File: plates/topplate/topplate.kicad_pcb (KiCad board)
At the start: 2 copper layers, 107.2 x 83.2 mm, 3 parts

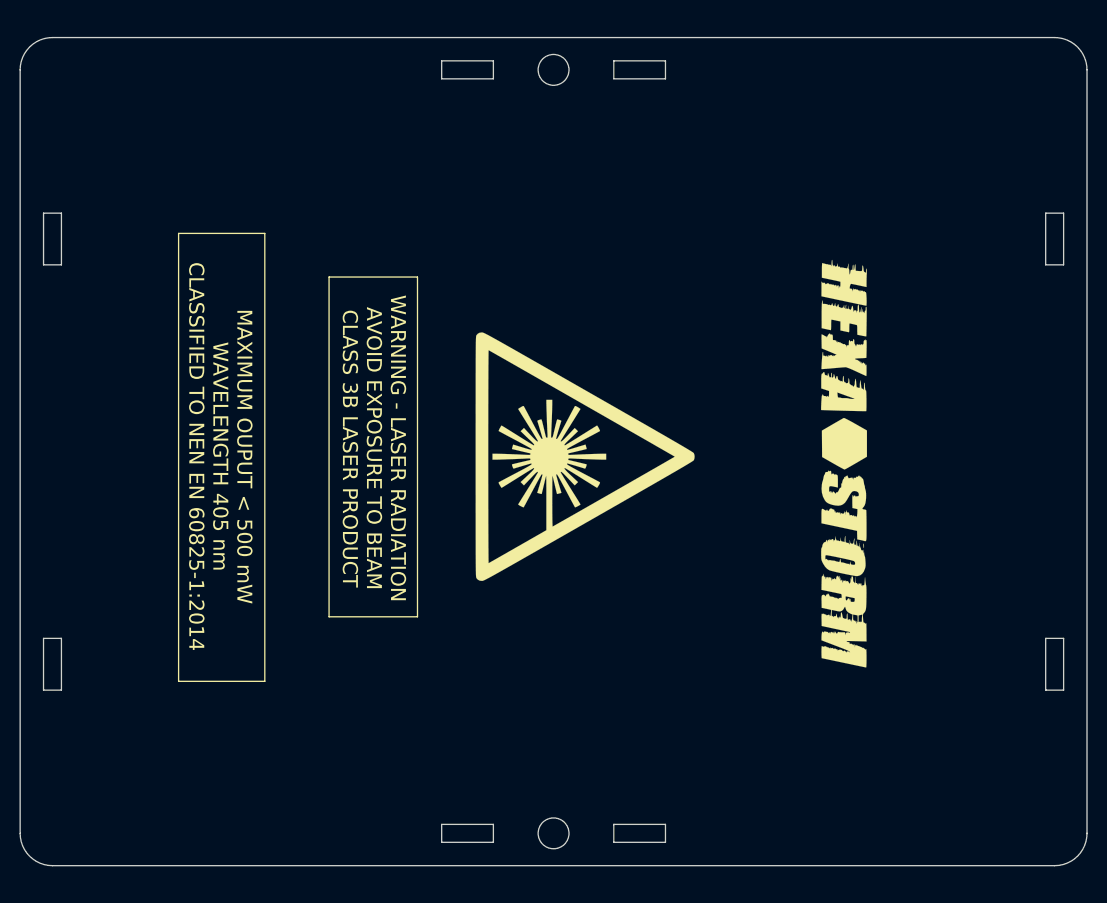
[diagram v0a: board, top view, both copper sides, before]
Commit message: improved bom changed export settings
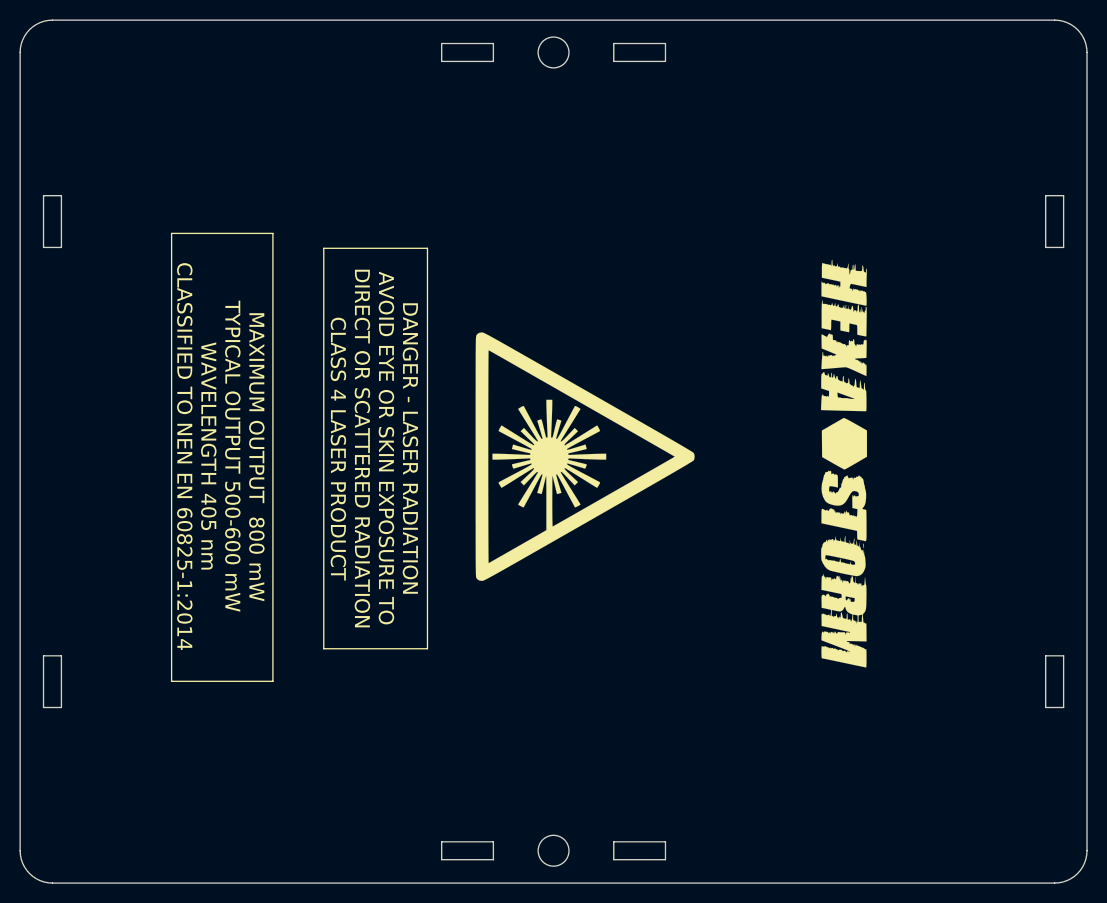
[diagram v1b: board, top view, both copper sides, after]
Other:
- board size 107.2 x 83.2 mm -> 107.2 x 86.7 mm
- board text added: "DANGER - LASER RADIATION AVOID EYE OR SKIN EXPOSURE TO DIRECT OR SCATTERED RADIATION CLASS 4 LASER PRODUCT"
- board text added: "MAXIMUM OUTPUT 800 mW TYPICAL OUTPUT 500-600 mW WAVELENGTH 405 nm CLASSIFIED TO NEN EN 60825-1:2014"
- board text removed: "MAXIMUM OUPUT < 500 mW WAVELENGTH 405 nm CLASSIFIED TO NEN EN 60825-1:2014"
- board text removed: "WARNING - LASER RADIATION AVOID EXPOSURE TO BEAM CLASS 3B LASER PRODUCT"

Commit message: added design of june
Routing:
- net (no net): vias 0 -> 2
- added copper zone on B.Cu, net (none)
- added copper zone on F.Cu, net (none)
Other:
- board size 107.2 x 86.7 mm -> 89 x 60 mm
- net class Default removed
- board text added: "HEXASTORM"
